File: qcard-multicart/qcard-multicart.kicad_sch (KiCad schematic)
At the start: 7 parts, among them J1 Conn_02x18_Top_Bottom, SW1 SW_DIP_x04, U1 MX29LV640EBTI-70G

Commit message: First pass at multicart
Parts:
- added C1, C2: 1uF, Capacitor_SMD:C_0805_2012Metric_Pad1.18x1.45mm_HandSolder, symbol Device:C
- added C3: 100pF, Capacitor_SMD:C_0805_2012Metric_Pad1.18x1.45mm_HandSolder, symbol Device:C
- added U2: MIC5365-3.3YD5, Package_TO_SOT_SMD:SOT-23-5, symbol Regulator_Linear:MIC5365-3.3YD5
- J1: footprint REB_Edge:REB_EdgeConnector_36pin -> reb-edge:REB_EdgeConnector_36pin
- R1, R2, R3, R4: footprint (none) -> Resistor_SMD:R_0805_2012Metric_Pad1.20x1.40mm_HandSolder
- SW1: footprint (none) -> Package_DIP:DIP-8_W7.62mm
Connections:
- net +3.3V: now also C2.1, C3.2, U2.5 (VOUT); no longer U1.30 (Q8), U1.32 (Q9), U1.34 (Q10), U1.36 (Q11), U1.39 (Q12), U1.41 (Q13), U1.43 (Q14), U1.47 (BYTE#)
- net +5V: now also C1.1, U2.1 (VIN), U2.3 (EN)
- net GND: now also U1.47 (BYTE#), C1.2, C2.2, C3.1, U2.2 (GND)
- no-connect marks 1 -> 8

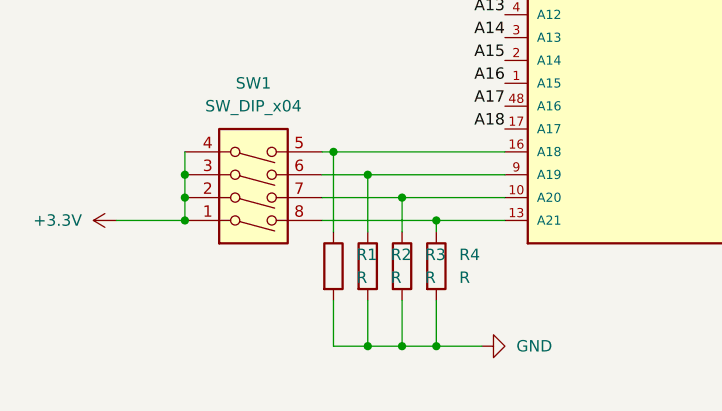
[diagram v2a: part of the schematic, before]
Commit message: changing pulldown to pullup
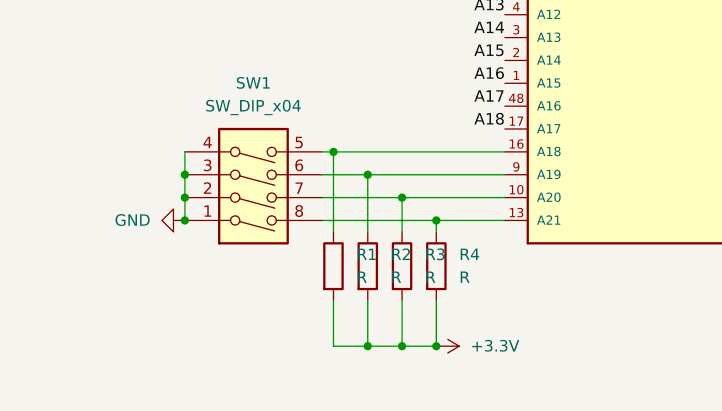
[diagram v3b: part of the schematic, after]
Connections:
- net +3.3V: now also R1.2, R2.2, R3.2, R4.2; no longer SW1.1, SW1.2, SW1.3, SW1.4
- net GND: now also SW1.1, SW1.2, SW1.3, SW1.4; no longer R1.2, R2.2, R3.2, R4.2
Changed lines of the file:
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@@
   (junction (at 77.47 118.11) (diameter 0) (color 0 0 0 0)
   )
-  (junction (at 77.47 120.65) (diameter 0) (color 0 0 0 0)
+  (junction (at 105.41 134.62) (diameter 0) (color 0 0 0 0)
   )
   (junction (at 158.75 120.65) (diameter 0) (color 0 0 0 0)
@@
   (junction (at 201.93 92.71) (diameter 0) (color 0 0 0 0)
   )
-  (junction (at 105.41 134.62) (diameter 0) (color 0 0 0 0)
-  )
   (junction (at 195.58 88.9) (diameter 0) (color 0 0 0 0)
   )
@@
   (junction (at 97.79 115.57) (diameter 0) (color 0 0 0 0)
   )
+  (junction (at 77.47 120.65) (diameter 0) (color 0 0 0 0)
+  )
   (junction (at 105.41 120.65) (diameter 0) (color 0 0 0 0)
   )
@@
     (stroke (width 0) (type default) (color 0 0 0 0))
   )
-  (wire (pts (xy 105.41 134.62) (xy 110.49 134.62))
-    (stroke (width 0) (type default) (color 0 0 0 0))
-  )
   (wire (pts (xy 181.61 114.3) (xy 186.69 114.3))
     (stroke (width 0) (type default) (color 0 0 0 0))
@@
     (stroke (width 0) (type default) (color 0 0 0 0))
   )
-  (wire (pts (xy 69.85 120.65) (xy 77.47 120.65))
-    (stroke (width 0) (type default) (color 0 0 0 0))
-  )
   (wire (pts (xy 208.28 88.9) (xy 208.28 92.71))
     (stroke (width 0) (type default) (color 0 0 0 0))
@@
     (pin "1")
   )
-  (symbol (lib_id "power:+3.3V") (at 69.85 120.65 90) (unit 1)
-    (in_bom yes) (on_board yes) (fields_autoplaced)
-    (property "Reference" "#PWR0108" (id 0) (at 73.66 120.65 0)
+  (symbol (lib_id "power:+3.3V") (at 105.41 134.62 270) (unit 1)
+    (in_bom yes) (on_board yes)
+    (property "Reference" "#PWR0108" (id 0) (at 101.6 134.62 0)
       (effects (font (size 1.27 1.27)) hide)
     )
-    (property "Value" "+3.3V" (id 1) (at 66.04 120.6499 90)
+    (property "Value" "+3.3V" (id 1) (at 109.22 134.6201 90)
       (effects (font (size 1.27 1.27)) (justify left))
     )
-    (property "Footprint" "" (id 2) (at 69.85 120.65 0)
+    (property "Footprint" "" (id 2) (at 105.41 134.62 0)
       (effects (font (size 1.27 1.27)) hide)
     )
-    (property "Datasheet" "" (id 3) (at 69.85 120.65 0)
+    (property "Datasheet" "" (id 3) (at 105.41 134.62 0)
       (effects (font (size 1.27 1.27)) hide)
     )
     (pin "1")
   )
-  (symbol (lib_id "power:GND") (at 110.49 134.62 90) (unit 1)
+  (symbol (lib_id "power:GND") (at 77.47 120.65 270) (unit 1)
     (in_bom yes) (on_board yes) (fields_autoplaced)
-    (property "Reference" "#PWR0104" (id 0) (at 116.84 134.62 0)
+    (property "Reference" "#PWR0104" (id 0) (at 71.12 120.65 0)
       (effects (font (size 1.27 1.27)) hide)
     )
-    (property "Value" "GND" (id 1) (at 114.3 134.6199 90)
+    (property "Value" "GND" (id 1) (at 73.66 120.6501 90)
       (effects (font (size 1.27 1.27)) (justify right))
     )
-    (property "Footprint" "" (id 2) (at 110.49 134.62 0)
+    (property "Footprint" "" (id 2) (at 77.47 120.65 0)
       (effects (font (size 1.27 1.27)) hide)
     )
-    (property "Datasheet" "" (id 3) (at 110.49 134.62 0)
+    (property "Datasheet" "" (id 3) (at 77.47 120.65 0)
       (effects (font (size 1.27 1.27)) hide)
     )

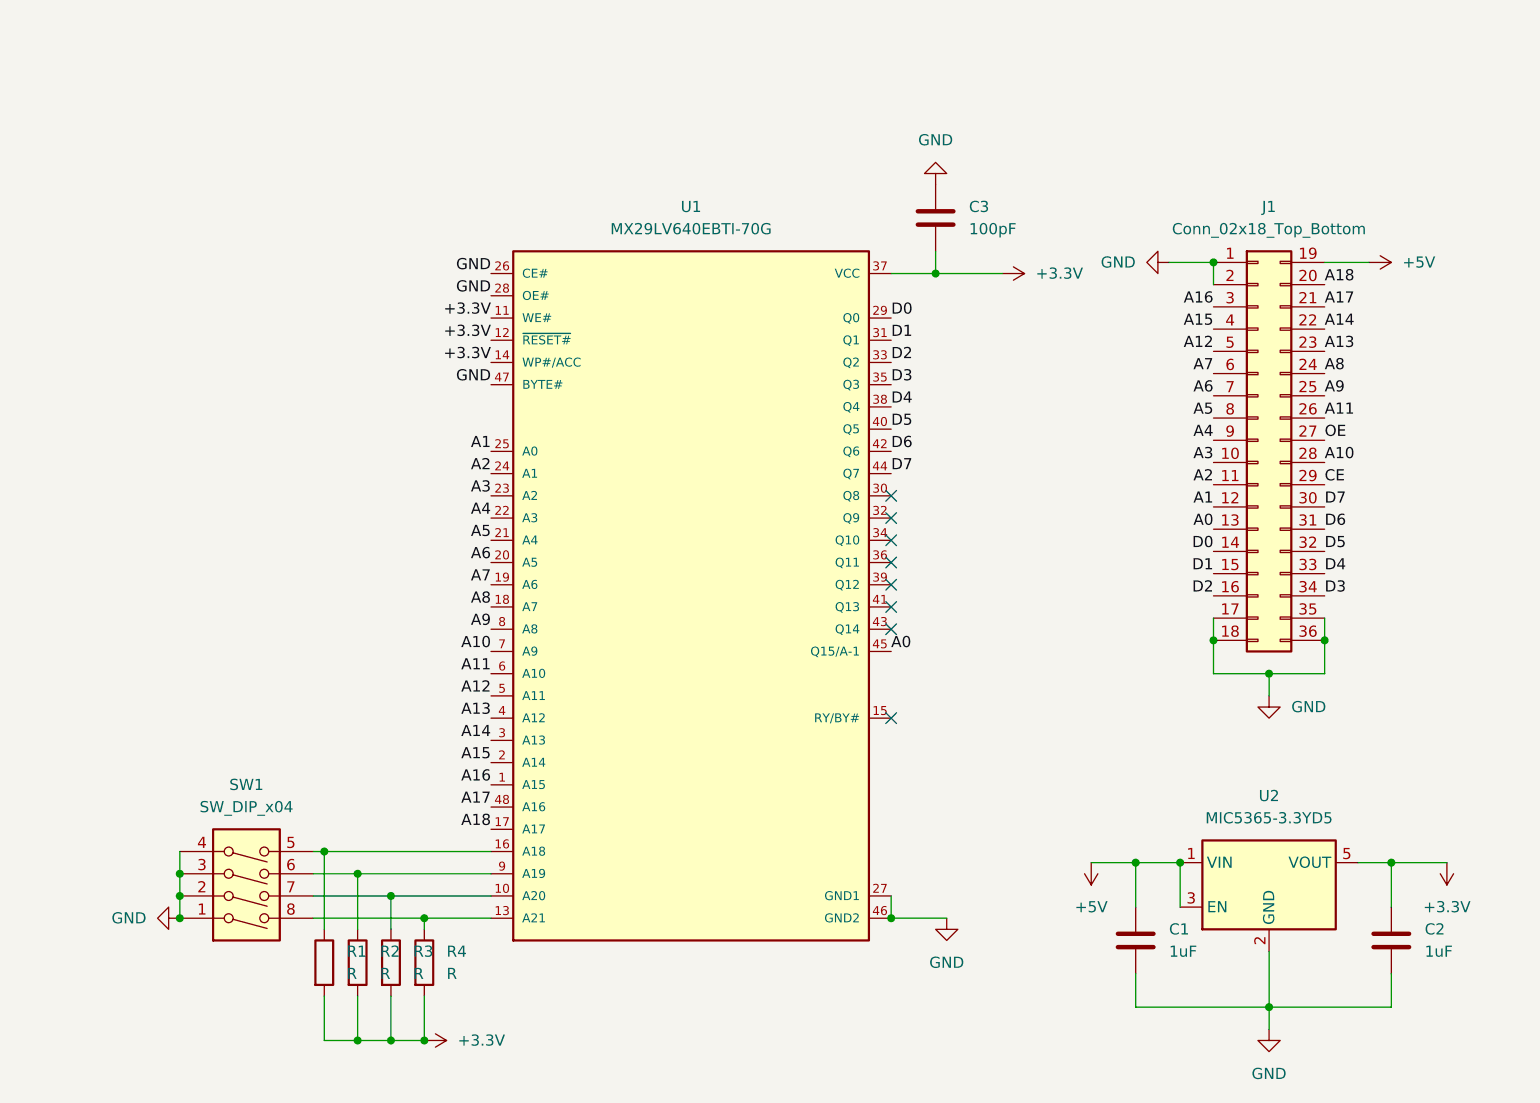
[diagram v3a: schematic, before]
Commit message: Multicart: connect OE/CE instead of always on, solve some DRC violations
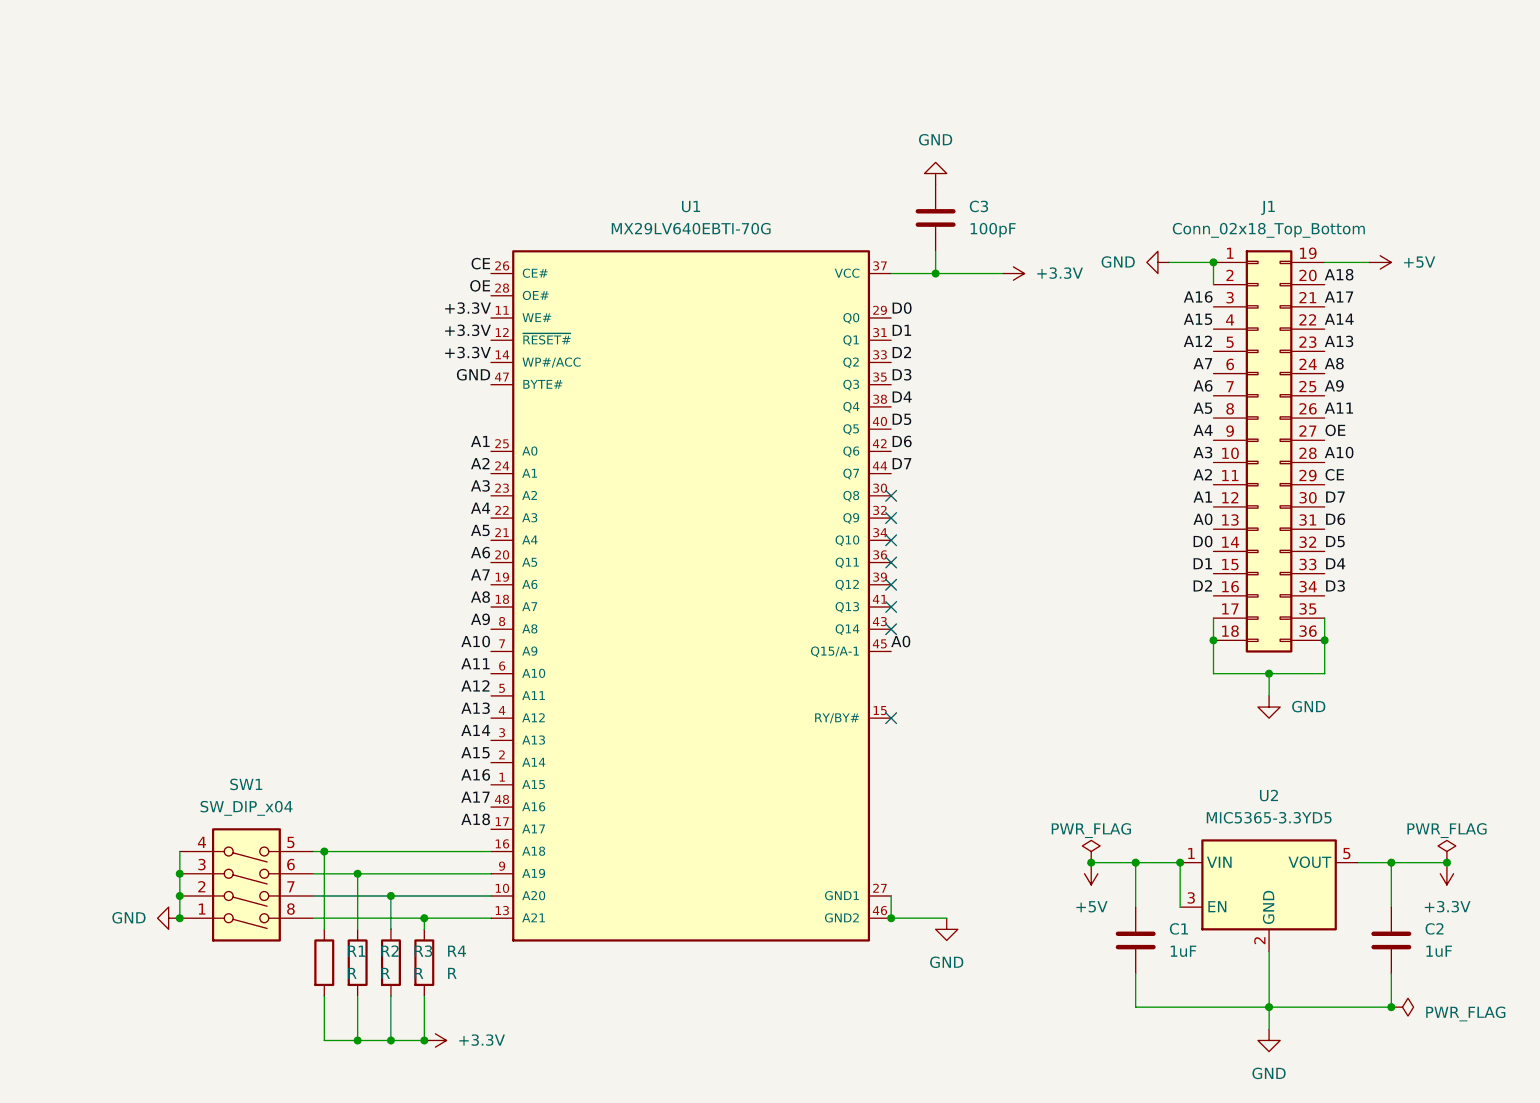
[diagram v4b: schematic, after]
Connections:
- net CE: now also U1.26 (CE#)
- net GND: no longer U1.26 (CE#), U1.28 (OE#)
- net OE: now also U1.28 (OE#)

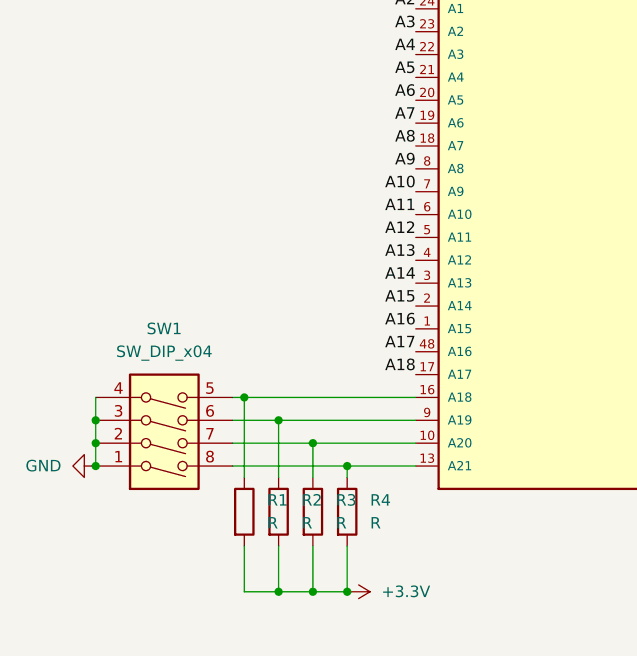
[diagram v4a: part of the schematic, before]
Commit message: Refactor multicart to use SMD resistor array for ease of assembly
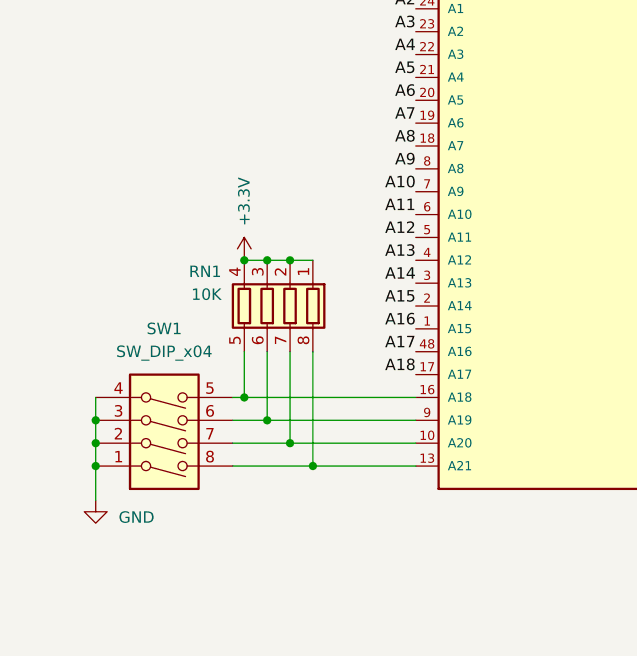
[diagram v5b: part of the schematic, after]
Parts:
- removed R1, R2, R3, R4: R, Resistor_SMD:R_0805_2012Metric_Pad1.20x1.40mm_HandSolder, symbol Device:R
- added RN1: 10K, Resistor_SMD:R_Array_Convex_4x0612, symbol Device:R_Pack04
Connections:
- net +3.3V: now also RN1.1 (R1.1), RN1.2 (R2.1), RN1.3 (R3.1), RN1.4 (R4.1)
- net at SW1.7, U1.10 (A20): now also RN1.7 (R2.2)
- net at SW1.8, U1.13 (A21): now also RN1.8 (R1.2)
- net at SW1.5, U1.16 (A18): now also RN1.5 (R4.2)
- net at SW1.6, U1.9 (A19): now also RN1.6 (R3.2)

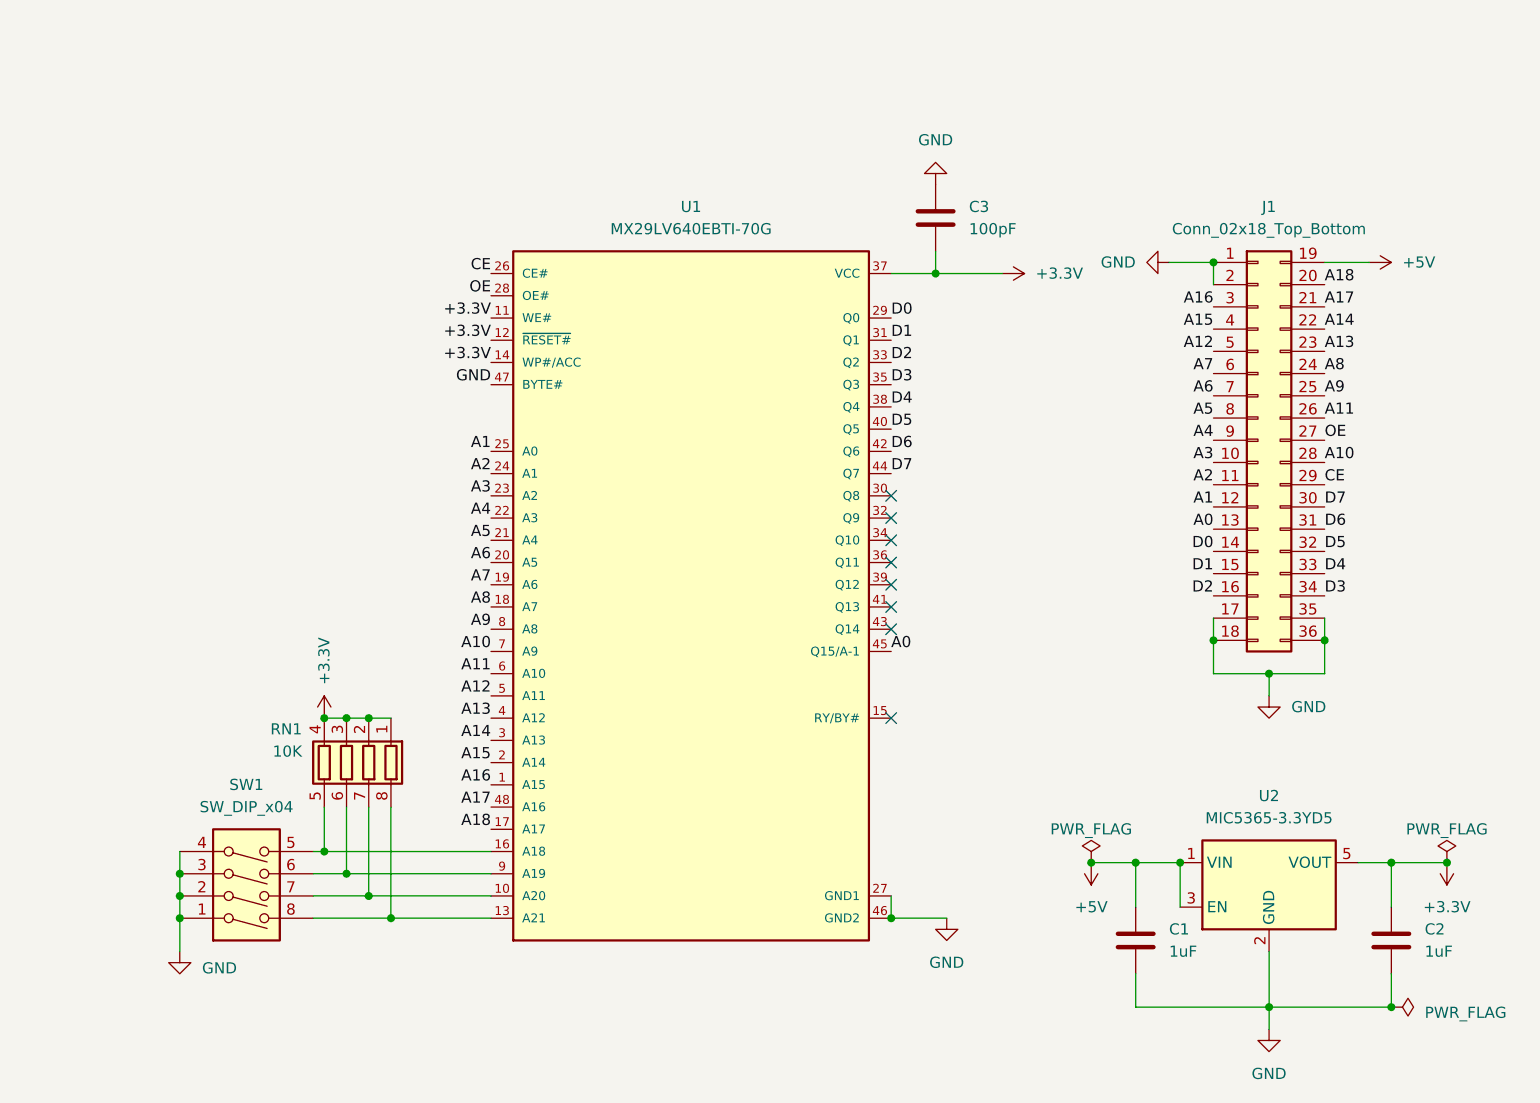
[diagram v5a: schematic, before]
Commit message: Removes resistor pack, current limits pulled up inputs
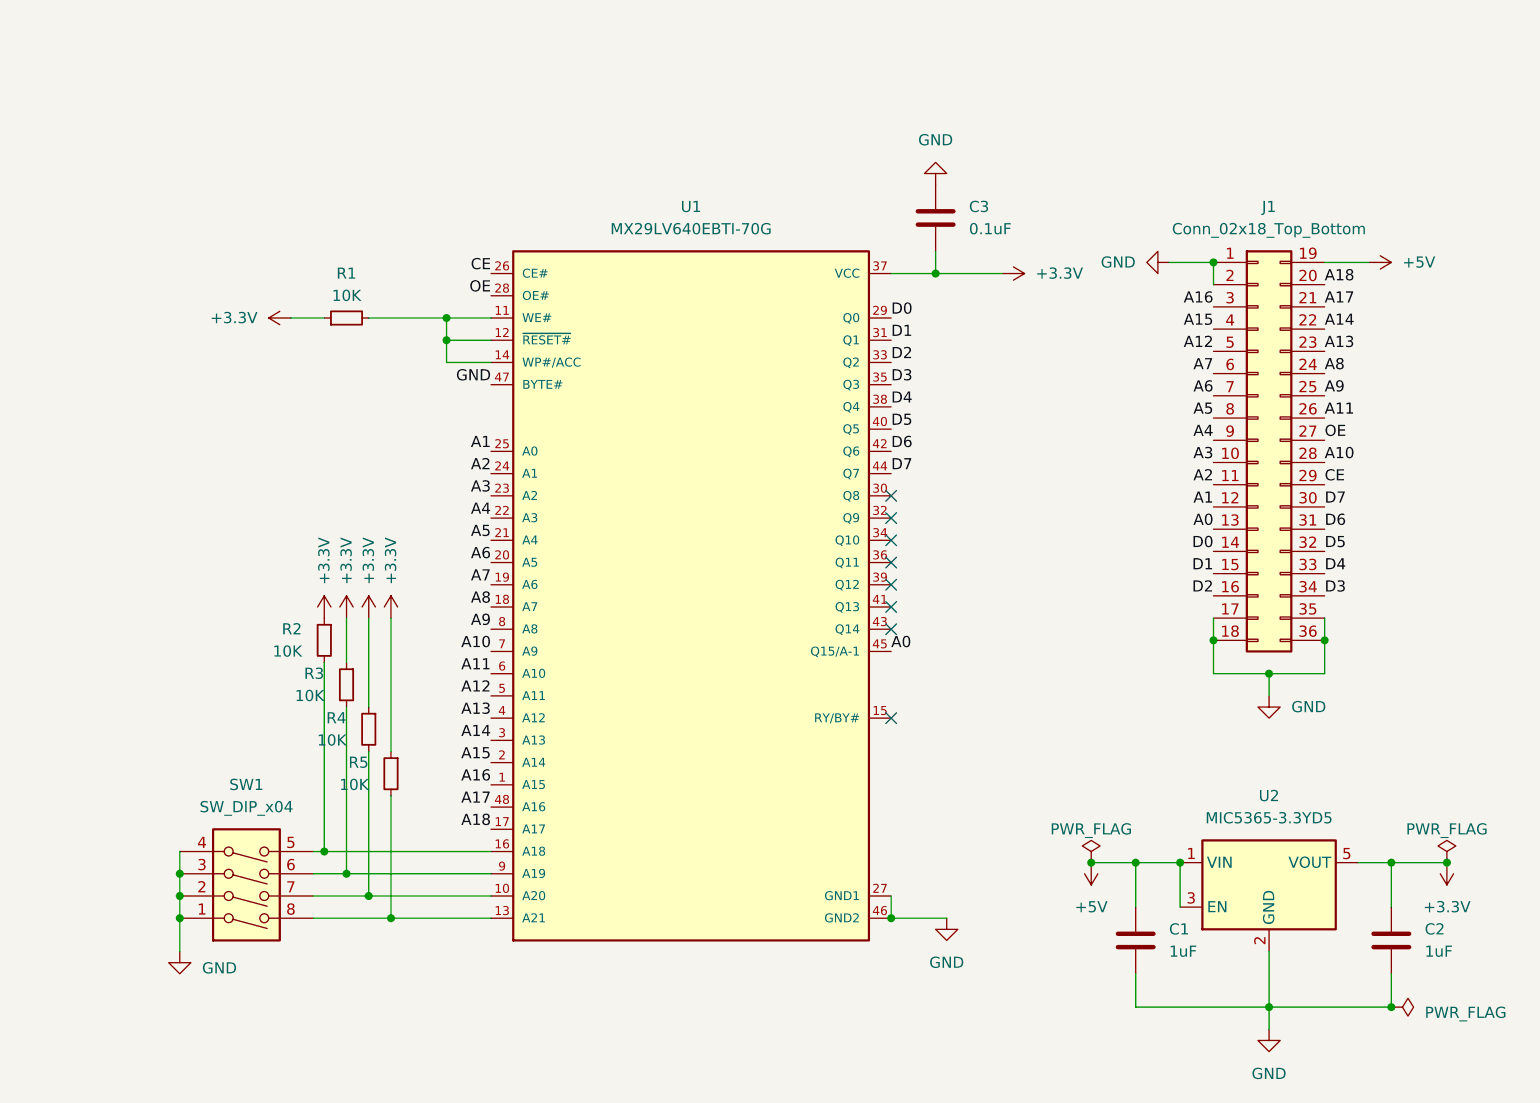
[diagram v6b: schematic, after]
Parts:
- removed RN1: 10K, Resistor_SMD:R_Array_Convex_4x0612, symbol Device:R_Pack04
- added R1, R2, R3, R4, R5: 10K, Resistor_SMD:R_0805_2012Metric_Pad1.20x1.40mm_HandSolder, symbol Device:R_Small
- C3: value 100pF -> 0.1uF
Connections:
- net +3.3V: now also R1.1, R2.1, R3.1, R4.1, R5.1; no longer U1.11 (WE#), U1.12 (~{RESET#}), U1.14 (WP#/ACC)
- net at SW1.5, U1.16 (A18): now also R2.2
- net at SW1.6, U1.9 (A19): now also R3.2
- net at SW1.7, U1.10 (A20): now also R4.2
- net at SW1.8, U1.13 (A21): now also R5.2
- new net: R1.2, U1.11 (WE#), U1.12 (~{RESET#}), U1.14 (WP#/ACC)
